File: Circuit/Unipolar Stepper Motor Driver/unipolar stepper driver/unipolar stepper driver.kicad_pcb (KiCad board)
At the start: 2 copper layers, 78.7 x 43.2 mm, 20 parts, among them Q1 S8050, Q2 S8050, Q3 S8050, Q4 S8050

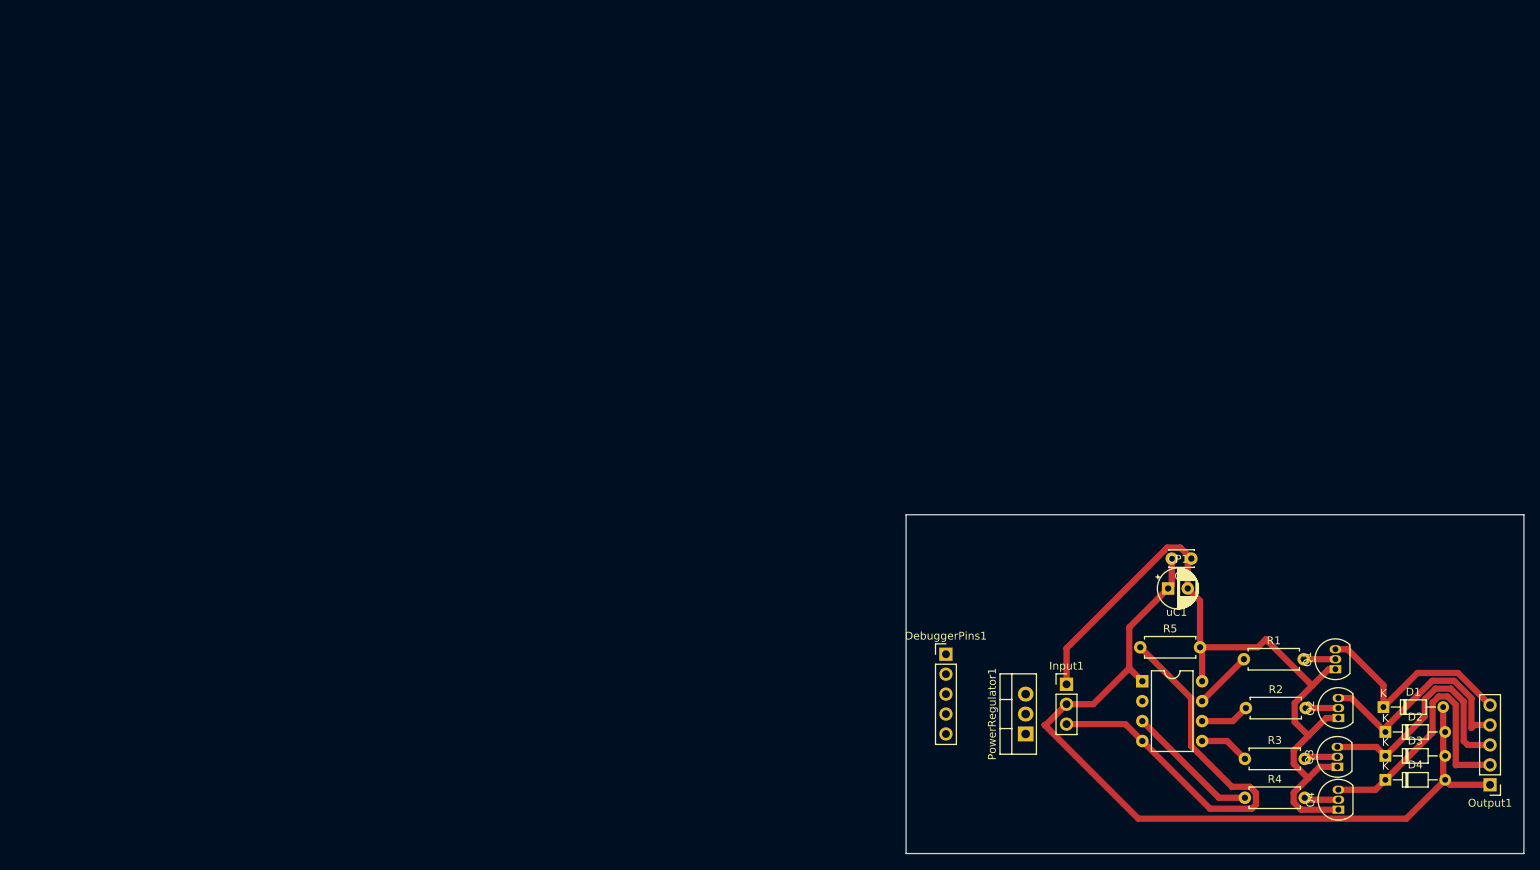
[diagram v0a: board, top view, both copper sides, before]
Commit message: Modified unipolar gerber file
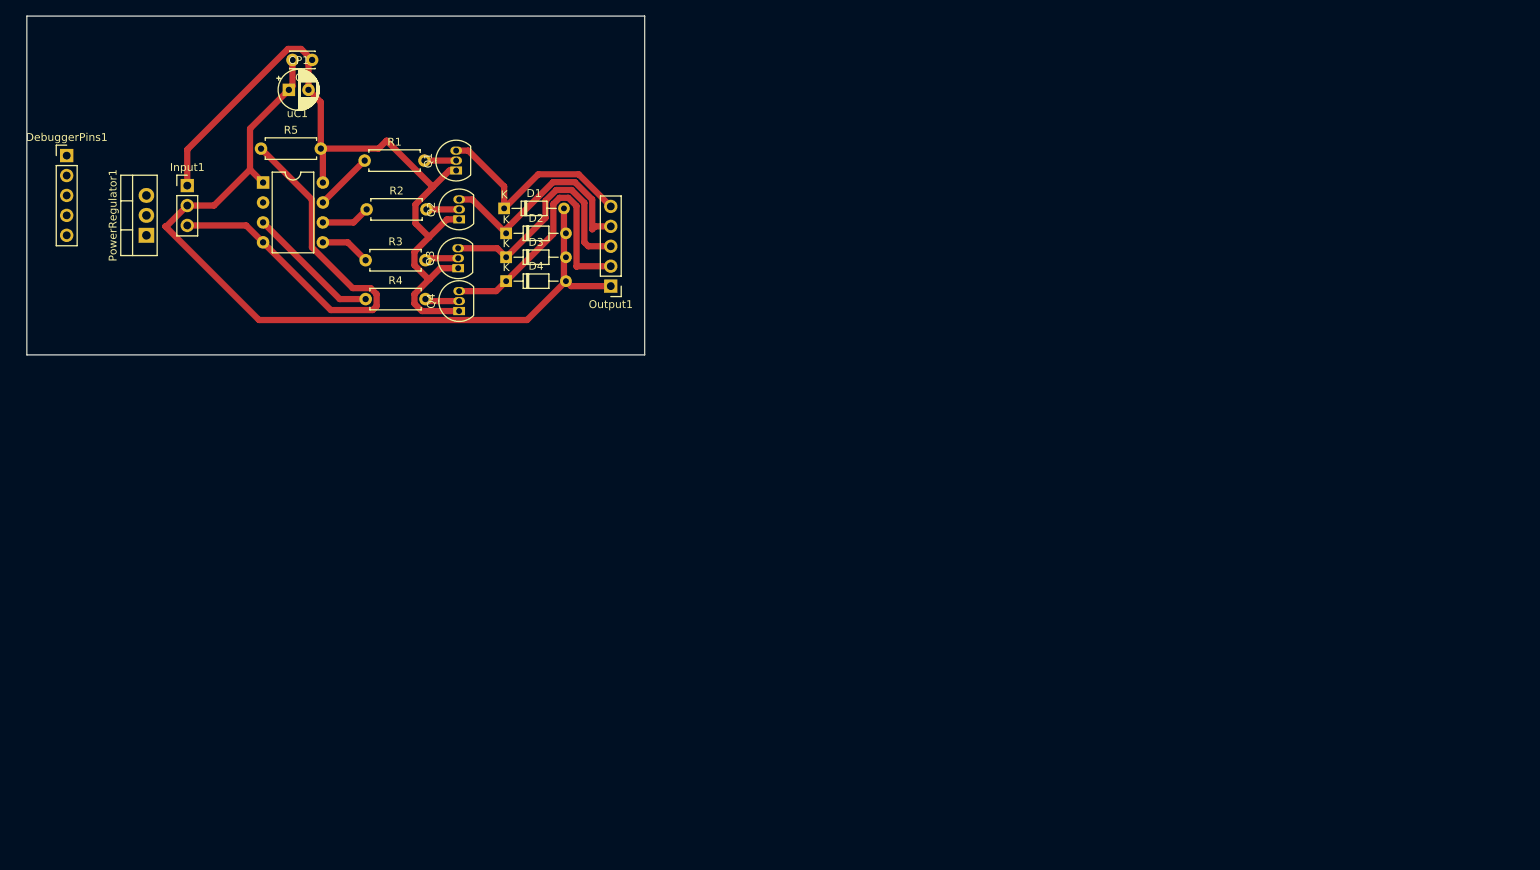
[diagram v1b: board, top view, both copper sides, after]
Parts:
- moved C1 128.8 mm to (48.8, 18.2)
- moved CP1 128.8 mm to (45.8, 22.0)
- moved D1 128.8 mm to (73.2, 37.2)
- moved D2 128.8 mm to (73.5, 40.3)
- moved D3 128.8 mm to (73.5, 43.4)
- moved D4 128.8 mm to (73.5, 46.4)
- moved Input1 128.8 mm to (32.9, 34.3)
- moved Output1 128.8 mm to (86.8, 47.1)
- moved Q3 128.8 mm to (67.4, 44.8)
- moved R1 128.8 mm to (55.5, 31.1)
- moved R2 128.8 mm to (55.7, 37.3)
- moved R5 128.8 mm to (42.2, 29.5)
- moved DebuggerPins1 128.8 mm to (17.5, 30.4)
- moved PowerRegulator1 128.8 mm to (27.6, 40.6)
- moved Q1 128.8 mm to (67.1, 32.3)
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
